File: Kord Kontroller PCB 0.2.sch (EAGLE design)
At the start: 188 parts, among them IC2 74HCT1G125DBV, J1 MIDIOUTB, J2 MIDIOUTA, J3 FTSH-105-01-L-DV-KJ, SW2 SPST_TACT-KMR2, U1 AP2112K-3.3, U2 ATSAMD51J19A-AUT, X3 microUSB

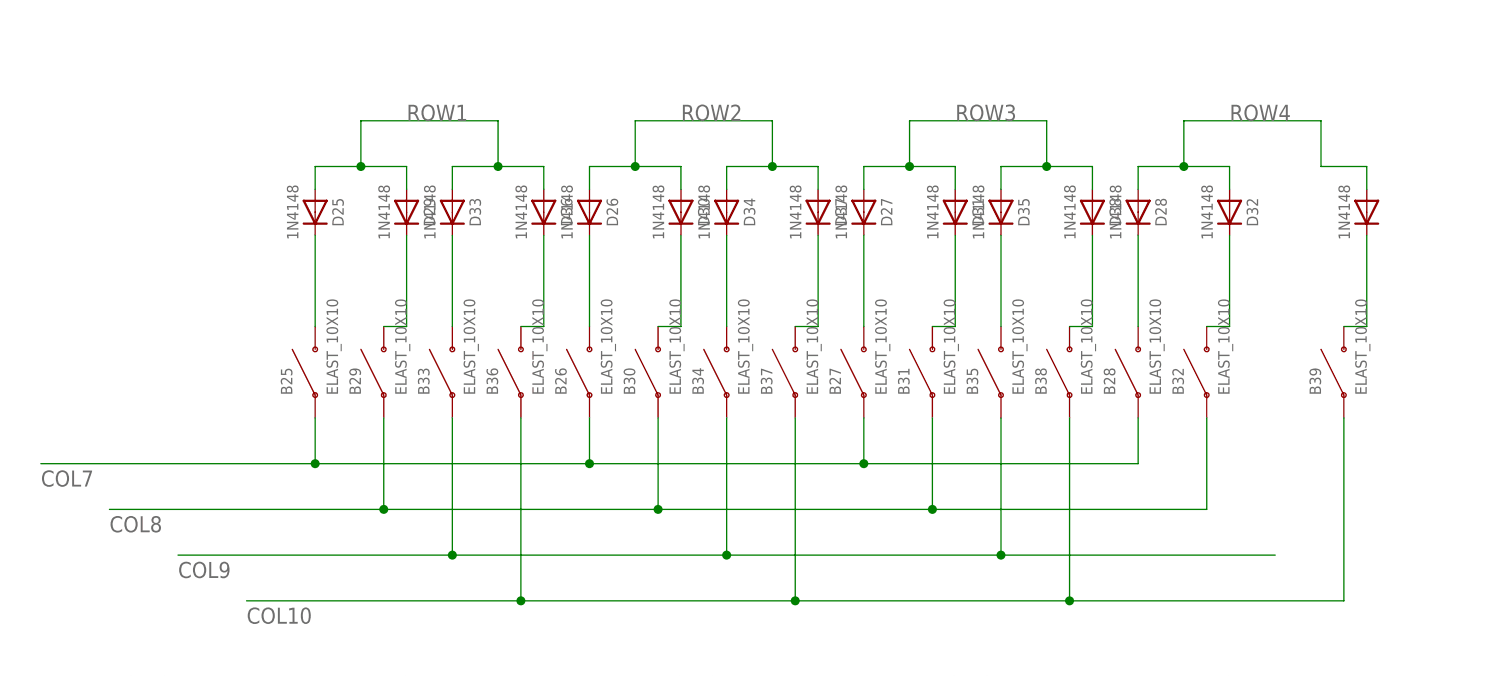
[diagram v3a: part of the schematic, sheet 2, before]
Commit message: Added Routes for Cols 0-6, Finished Rows and diodes
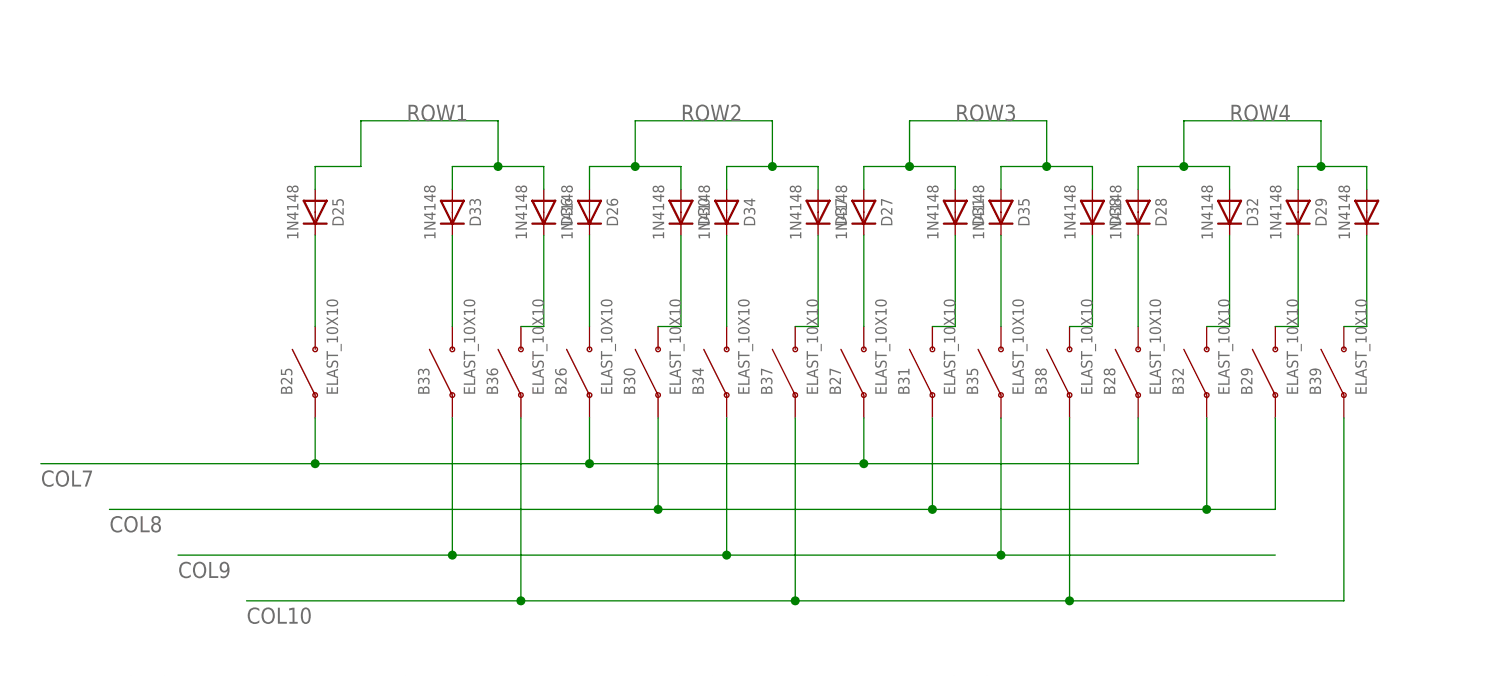
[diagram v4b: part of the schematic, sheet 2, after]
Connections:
- net COL0: now also U2.PB15/EIC/EXTINT[15]; no longer U2.PA00/EIC/EXTINT[0]
- net COL1: now also U2.PB14//EIC/EXTINT[14]; no longer U2.PA01/EIC/EXTINT[1]
- net COL2: now also U2.PB13/EIC/EXTINT[13]; no longer U2.PA02/EIC/EXTINT[2]/ADC0/AIN[0]/DAC
- net COL3: now also U2.PB12/EIC/EXTINT[12]; no longer U2.PA03/EIC/EXTINT[3]/ANAREF/VREFA/ADC0/ADIN[1]
- net COL4: now also U2.PA11/EIC/EXTINT[11]/ADC0/AIN[11]; no longer U2.PA04/EIC/EXTINT[4]/ANAREF/VREFB/ADOC0/AIN[4]
- net COL5: now also U2.PA10//EIC/EXTINT[10]/ADC0/AIN[10]; no longer U2.PA05//EIC/EXTINT[5]/ADC0/AIN[5]
- net COL6: now also U2.PA09/EIC/EXTINT[9]/ADC0/AIN[9]/ADC1/AIN[3]; no longer U2.PA06/EIC/EXTINT[6]/ANAREF/VREFC/ADC0/AIN[6]
- net ROW1: no longer D29.A
- net ROW4: now also D29.A, U2.PA15/EIC/EXTINT[15]; no longer U2.PB11//EIC/EXTINT[11]
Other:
- moved on the sheet: B29, D29
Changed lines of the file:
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@@
 <part name="FRAME1" library="SparkFun-Aesthetics" deviceset="FRAME-LEDGER" device=""/>
 <part name="D25" library="microbuilder" deviceset="DIODE" device="SOD-323" value="1N4148"/>
-<part name="D29" library="microbuilder" deviceset="DIODE" device="SOD-323" value="1N4148"/>
 <part name="D33" library="microbuilder" deviceset="DIODE" device="SOD-323" value="1N4148"/>
 <part name="D36" library="microbuilder" deviceset="DIODE" device="SOD-323" value="1N4148"/>
@@
 <part name="D38" library="microbuilder" deviceset="DIODE" device="SOD-323" value="1N4148"/>
 <part name="B25" library="microbuilder" deviceset="ELAST_10X10" device=""/>
-<part name="B29" library="microbuilder" deviceset="ELAST_10X10" device=""/>
 <part name="B33" library="microbuilder" deviceset="ELAST_10X10" device=""/>
 <part name="B36" library="microbuilder" deviceset="ELAST_10X10" device=""/>
@@
 <part name="R7" library="microbuilder" deviceset="RESISTOR" device="_0603_NOOUT" value="10K"/>
 <part name="U$7" library="microbuilder" deviceset="3.3V" device=""/>
+<part name="D29" library="microbuilder" deviceset="DIODE" device="SOD-323" value="1N4148"/>
+<part name="B29" library="microbuilder" deviceset="ELAST_10X10" device=""/>
 </parts>
 <sheets>
@@
 <net name="COL3" class="0">
 <segment>
-<wire x1="652.78" y1="-30.48" x2="665.48" y2="-30.48" width="0.1524" layer="91"/>
-<label x="655.32" y="-30.48" size="1.778" layer="95"/>
-<pinref part="U2" gate="G$1" pin="PA03/EIC/EXTINT[3]/ANAREF/VREFA/ADC0/ADIN[1]"/>
+<wire x1="789.94" y1="-45.72" x2="777.24" y2="-45.72" width="0.1524" layer="91"/>
+<label x="787.4" y="-43.18" size="1.778" layer="95" rot="R180"/>
+<pinref part="U2" gate="G$1" pin="PB12/EIC/EXTINT[12]"/>
 </segment>
 </net>
 <net name="COL2" class="0">
 <segment>
-<wire x1="652.78" y1="-27.94" x2="665.48" y2="-27.94" width="0.1524" layer="91"/>
-<label x="655.32" y="-27.94" size="1.778" layer="95"/>
-<pinref part="U2" gate="G$1" pin="PA02/EIC/EXTINT[2]/ADC0/AIN[0]/DAC"/>
+<wire x1="789.94" y1="-43.18" x2="777.24" y2="-43.18" width="0.1524" layer="91"/>
+<label x="787.4" y="-40.64" size="1.778" layer="95" rot="R180"/>
+<pinref part="U2" gate="G$1" pin="PB13/EIC/EXTINT[13]"/>
 </segment>
 </net>
 <net name="COL1" class="0">
 <segment>
-<wire x1="665.48" y1="-25.4" x2="652.78" y2="-25.4" width="0.1524" layer="91"/>
-<label x="655.32" y="-25.4" size="1.778" layer="95"/>
-<pinref part="U2" gate="G$1" pin="PA01/EIC/EXTINT[1]"/>
+<wire x1="777.24" y1="-40.64" x2="789.94" y2="-40.64" width="0.1524" layer="91"/>
+<label x="787.4" y="-38.1" size="1.778" layer="95" rot="R180"/>
+<pinref part="U2" gate="G$1" pin="PB14//EIC/EXTINT[14]"/>
 </segment>
 </net>
 <net name="COL0" class="0">
 <segment>
-<wire x1="652.78" y1="-22.86" x2="665.48" y2="-22.86" width="0.1524" layer="91"/>
-<label x="655.32" y="-22.86" size="1.778" layer="95"/>
-<pinref part="U2" gate="G$1" pin="PA00/EIC/EXTINT[0]"/>
+<wire x1="789.94" y1="-38.1" x2="777.24" y2="-38.1" width="0.1524" layer="91"/>
+<label x="787.4" y="-35.56" size="1.778" layer="95" rot="R180"/>
+<pinref part="U2" gate="G$1" pin="PB15/EIC/EXTINT[15]"/>
 </segment>
 </net>
@@
 <net name="COL4" class="0">
 <segment>
-<wire x1="652.78" y1="-33.02" x2="665.48" y2="-33.02" width="0.1524" layer="91"/>
-<label x="655.32" y="-33.02" size="1.778" layer="95"/>
-<pinref part="U2" gate="G$1" pin="PA04/EIC/EXTINT[4]/ANAREF/VREFB/ADOC0/AIN[4]"/>
+<wire x1="652.78" y1="-50.8" x2="665.48" y2="-50.8" width="0.1524" layer="91"/>
+<label x="655.32" y="-50.8" size="1.778" layer="95"/>
+<pinref part="U2" gate="G$1" pin="PA11/EIC/EXTINT[11]/ADC0/AIN[11]"/>
 </segment>
 </net>
 <net name="COL5" class="0">
 <segment>
-<wire x1="652.78" y1="-35.56" x2="665.48" y2="-35.56" width="0.1524" layer="91"/>
-<label x="655.32" y="-35.56" size="1.778" layer="95"/>
-<pinref part="U2" gate="G$1" pin="PA05//EIC/EXTINT[5]/ADC0/AIN[5]"/>
+<wire x1="652.78" y1="-48.26" x2="665.48" y2="-48.26" width="0.1524" layer="91"/>
+<label x="655.32" y="-48.26" size="1.778" layer="95"/>
+<pinref part="U2" gate="G$1" pin="PA10//EIC/EXTINT[10]/ADC0/AIN[10]"/>
 </segment>
 </net>
 <net name="COL6" class="0">
 <segment>
-<wire x1="652.78" y1="-38.1" x2="665.48" y2="-38.1" width="0.1524" layer="91"/>
-<label x="655.32" y="-38.1" size="1.778" layer="95"/>
-<pinref part="U2" gate="G$1" pin="PA06/EIC/EXTINT[6]/ANAREF/VREFC/ADC0/AIN[6]"/>
+<wire x1="652.78" y1="-45.72" x2="665.48" y2="-45.72" width="0.1524" layer="91"/>
+<label x="655.32" y="-45.72" size="1.778" layer="95"/>
+<pinref part="U2" gate="G$1" pin="PA09/EIC/EXTINT[9]/ADC0/AIN[9]/ADC1/AIN[3]"/>
 </segment>
 </net>
@@
 <net name="ROW4" class="0">
 <segment>
-<wire x1="777.24" y1="-48.26" x2="789.94" y2="-48.26" width="0.1524" layer="91"/>
-<label x="779.78" y="-48.26" size="1.778" layer="95"/>
-<pinref part="U2" gate="G$1" pin="PB11//EIC/EXTINT[11]"/>
+<wire x1="652.78" y1="-60.96" x2="665.48" y2="-60.96" width="0.1524" layer="91"/>
+<label x="655.32" y="-60.96" size="1.778" layer="95"/>
+<pinref part="U2" gate="G$1" pin="PA15/EIC/EXTINT[15]"/>
 </segment>
 </net>
@@
 <attribute name="VALUE" x="76.24" y="220.98" size="1.27" layer="96" rot="R270" align="center"/>
 </instance>
-<instance part="D29" gate="G$1" x="88.9" y="220.98" smashed="yes" rot="R270">
-<attribute name="NAME" x="91.44" y="220.98" size="1.27" layer="95" rot="R270" align="center"/>
-<attribute name="VALUE" x="86.4" y="220.98" size="1.27" layer="96" rot="R270" align="center"/>
-</instance>
 <instance part="D33" gate="G$1" x="93.98" y="220.98" smashed="yes" rot="R270">
 <attribute name="NAME" x="96.52" y="220.98" size="1.27" layer="95" rot="R270" align="center"/>
@@
 <attribute name="VALUE" x="81.28" y="200.66" size="1.27" layer="96" rot="R90"/>
 </instance>
-<instance part="B29" gate="G$1" x="86.36" y="203.2" smashed="yes" rot="R90">
-<attribute name="NAME" x="83.82" y="200.66" size="1.27" layer="95" rot="R90"/>
-<attribute name="VALUE" x="88.9" y="200.66" size="1.27" layer="96" rot="R90"/>
-</instance>
 <instance part="B33" gate="G$1" x="93.98" y="203.2" smashed="yes" rot="R90">
 <attribute name="NAME" x="91.44" y="200.66" size="1.27" layer="95" rot="R90"/>
@@
 <attribute name="VALUE" x="193.04" y="137.16" size="1.27" layer="96" rot="R90"/>
 </instance>
+<instance part="D29" gate="G$1" x="187.96" y="220.98" smashed="yes" rot="R270">
+<attribute name="NAME" x="190.5" y="220.98" size="1.27" layer="95" rot="R270" align="center"/>
+<attribute name="VALUE" x="185.46" y="220.98" size="1.27" layer="96" rot="R270" align="center"/>
+</instance>
+<instance part="B29" gate="G$1" x="185.42" y="203.2" smashed="yes" rot="R90">
+<attribute name="NAME" x="182.88" y="200.66" size="1.27" layer="95" rot="R90"/>
+<attribute name="VALUE" x="187.96" y="200.66" size="1.27" layer="96" rot="R90"/>
+</instance>
 </instances>
 <busses>
@@
 <wire x1="78.74" y1="223.52" x2="78.74" y2="226.06" width="0.1524" layer="91"/>
 <wire x1="78.74" y1="226.06" x2="83.82" y2="226.06" width="0.1524" layer="91"/>
-<pinref part="D29" gate="G$1" pin="A"/>
-<wire x1="83.82" y1="226.06" x2="88.9" y2="226.06" width="0.1524" layer="91"/>
-<wire x1="88.9" y1="226.06" x2="88.9" y2="223.52" width="0.1524" layer="91"/>
 <wire x1="83.82" y1="231.14" x2="83.82" y2="226.06" width="0.1524" layer="91"/>
-<junction x="83.82" y="226.06"/>
 <pinref part="D33" gate="G$1" pin="A"/>
 <wire x1="93.98" y1="223.52" x2="93.98" y2="226.06" width="0.1524" layer="91"/>
@@
 <wire x1="175.26" y1="231.14" x2="175.26" y2="226.06" width="0.1524" layer="91"/>
 <junction x="175.26" y="226.06"/>
+<pinref part="D29" gate="G$1" pin="A"/>
+<wire x1="187.96" y1="226.06" x2="187.96" y2="223.52" width="0.1524" layer="91"/>
+<wire x1="187.96" y1="226.06" x2="190.5" y2="226.06" width="0.1524" layer="91"/>
+<junction x="190.5" y="226.06"/>
 </segment>
 <segment>
@@
 </segment>
 </net>
-<net name="N$74" class="0">
-<segment>
-<wire x1="86.36" y1="208.28" x2="88.9" y2="208.28" width="0.1524" layer="91"/>
-<wire x1="88.9" y1="208.28" x2="88.9" y2="218.44" width="0.1524" layer="91"/>
-<pinref part="D29" gate="G$1" pin="C"/>
-<pinref part="B29" gate="G$1" pin="P$2"/>
-</segment>
-</net>
 <net name="N$75" class="0">
 <segment>
@@
 <net name="COL8" class="0">
 <segment>
-<wire x1="55.88" y1="187.96" x2="86.36" y2="187.96" width="0.1524" layer="91"/>
-<wire x1="86.36" y1="187.96" x2="116.84" y2="187.96" width="0.1524" layer="91"/>
-<wire x1="86.36" y1="198.12" x2="86.36" y2="187.96" width="0.1524" layer="91"/>
-<junction x="86.36" y="187.96"/>
+<wire x1="55.88" y1="187.96" x2="116.84" y2="187.96" width="0.1524" layer="91"/>
 <wire x1="116.84" y1="198.12" x2="116.84" y2="187.96" width="0.1524" layer="91"/>
 <junction x="116.84" y="187.96"/>
 <label x="55.88" y="185.42" size="1.778" layer="95"/>
-<pinref part="B29" gate="G$1" pin="P$1"/>
 <pinref part="B30" gate="G$1" pin="P$1"/>
 <wire x1="116.84" y1="187.96" x2="147.32" y2="187.96" width="0.1524" layer="91"/>
@@
 <wire x1="147.32" y1="198.12" x2="147.32" y2="187.96" width="0.1524" layer="91"/>
 <junction x="147.32" y="187.96"/>
+<pinref part="B29" gate="G$1" pin="P$1"/>
+<wire x1="185.42" y1="198.12" x2="185.42" y2="187.96" width="0.1524" layer="91"/>
+<wire x1="185.42" y1="187.96" x2="177.8" y2="187.96" width="0.1524" layer="91"/>
+<junction x="177.8" y="187.96"/>
 </segment>
 </net>
@@
 </segment>
 </net>
+<net name="N$70" class="0">
+<segment>
+<wire x1="185.42" y1="208.28" x2="187.96" y2="208.28" width="0.1524" layer="91"/>
+<wire x1="187.96" y1="208.28" x2="187.96" y2="218.44" width="0.1524" layer="91"/>
+<pinref part="D29" gate="G$1" pin="C"/>
+<pinref part="B29" gate="G$1" pin="P$2"/>
+</segment>
+</net>
